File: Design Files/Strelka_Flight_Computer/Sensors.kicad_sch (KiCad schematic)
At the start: 0 parts

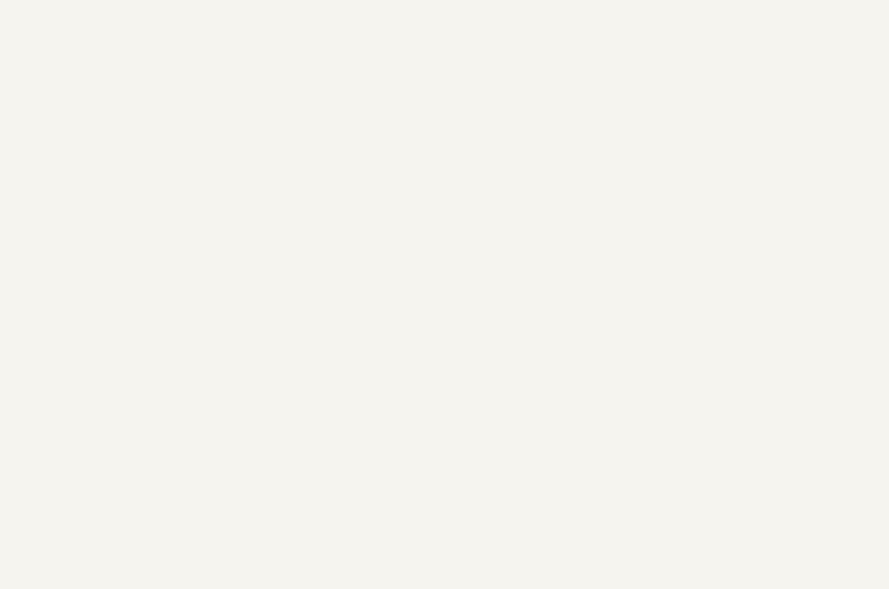
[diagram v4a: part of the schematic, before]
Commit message: Added new UBLOX GPS
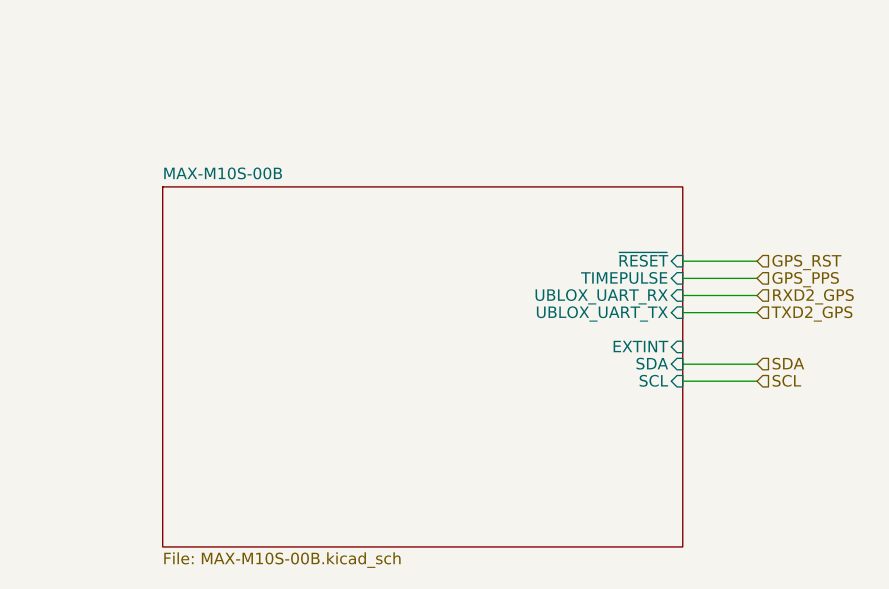
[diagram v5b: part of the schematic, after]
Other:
- added sheet MAX-M10S-00B (MAX-M10S-00B.kicad_sch)
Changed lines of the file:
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@@
+    (stroke (width 0) (type default) (color 0 0 0 0))
+  )
+  (wire (pts (xy 211.455 116.205) (xy 219.71 116.205))
     (stroke (width 0) (type default) (color 0 0 0 0))
   )
@@
     (stroke (width 0) (type default) (color 0 0 0 0))
   )
+  (wire (pts (xy 211.455 121.92) (xy 219.71 121.92))
+    (stroke (width 0) (type default) (color 0 0 0 0))
+  )
+  (wire (pts (xy 211.455 120.015) (xy 219.71 120.015))
+    (stroke (width 0) (type default) (color 0 0 0 0))
+  )
   (wire (pts (xy 95.25 41.275) (xy 103.505 41.275))
     (stroke (width 0) (type default) (color 0 0 0 0))
@@
     (stroke (width 0) (type default) (color 0 0 0 0))
   )
+  (wire (pts (xy 211.455 129.54) (xy 219.71 129.54))
+    (stroke (width 0) (type default) (color 0 0 0 0))
+  )
   (wire (pts (xy 95.25 134.62) (xy 103.505 134.62))
     (stroke (width 0) (type default) (color 0 0 0 0))
@@
     (stroke (width 0) (type default) (color 0 0 0 0))
   )
+  (wire (pts (xy 211.455 118.11) (xy 219.71 118.11))
+    (stroke (width 0) (type default) (color 0 0 0 0))
+  )
   (wire (pts (xy 211.455 43.815) (xy 219.71 43.815))
     (stroke (width 0) (type default) (color 0 0 0 0))
@@
     (stroke (width 0) (type default) (color 0 0 0 0))
   )
+  (wire (pts (xy 211.455 127.635) (xy 219.71 127.635))
+    (stroke (width 0) (type default) (color 0 0 0 0))
+  )
   (hierarchical_label "DATA_READY_MAG" (shape input) (at 103.505 136.525 0)
     (effects (font (size 1.27 1.27)) (justify left))
@@
     (effects (font (size 1.27 1.27)) (justify left))
   )
+  (hierarchical_label "RXD2_GPS" (shape input) (at 219.71 120.015 0)
+    (effects (font (size 1.27 1.27)) (justify left))
+  )
   (hierarchical_label "MOSI_BMX055" (shape input) (at 103.505 113.03 0)
     (effects (font (size 1.27 1.27)) (justify left))
@@
     (effects (font (size 1.27 1.27)) (justify left))
   )
+  (hierarchical_label "GPS_PPS" (shape input) (at 219.71 118.11 0)
+    (effects (font (size 1.27 1.27)) (justify left))
+  )
+  (hierarchical_label "SCL" (shape input) (at 219.71 129.54 0)
+    (effects (font (size 1.27 1.27)) (justify left))
+  )
+  (hierarchical_label "GPS_RST" (shape input) (at 219.71 116.205 0)
+    (effects (font (size 1.27 1.27)) (justify left))
+  )
+  (hierarchical_label "TXD2_GPS" (shape input) (at 219.71 121.92 0)
+    (effects (font (size 1.27 1.27)) (justify left))
+  )
   (hierarchical_label "GPS_PPS" (shape input) (at 219.71 41.91 0)
+    (effects (font (size 1.27 1.27)) (justify left))
+  )
+  (hierarchical_label "SDA" (shape input) (at 219.71 127.635 0)
     (effects (font (size 1.27 1.27)) (justify left))
   )
@@
       (effects (font (size 1.27 1.27)) (justify right))
     )
+  )
+  (sheet (at 153.67 107.95) (size 57.785 40.005) (fields_autoplaced)
+    (stroke (width 0.1524) (type solid) (color 0 0 0 0))
+    (fill (color 0 0 0 0.0000))
+    (property "Sheet name" "MAX-M10S-00B" (id 0) (at 153.67 107.2384 0)
+      (effects (font (size 1.27 1.27)) (justify left bottom))
+    )
+    (property "Sheet file" "MAX-M10S-00B.kicad_sch" (id 1) (at 153.67 148.5396 0)
+      (effects (font (size 1.27 1.27)) (justify left top))
+    )
+    (pin "SCL" input (at 211.455 129.54 0)
+      (effects (font (size 1.27 1.27)) (justify right))
+    )
+    (pin "SDA" input (at 211.455 127.635 0)
+      (effects (font (size 1.27 1.27)) (justify right))
+    )
+    (pin "UBLOX_UART_RX" input (at 211.455 120.015 0)
+      (effects (font (size 1.27 1.27)) (justify right))
+    )
+    (pin "~{RESET}" input (at 211.455 116.205 0)
+      (effects (font (size 1.27 1.27)) (justify right))
+    )
+    (pin "EXTINT" input (at 211.455 125.73 0)
+      (effects (font (size 1.27 1.27)) (justify right))
+    )
+    (pin "UBLOX_UART_TX" input (at 211.455 121.92 0)
+      (effects (font (size 1.27 1.27)) (justify right))
+    )
+    (pin "TIMEPULSE" input (at 211.455 118.11 0)
+      (effects (font (size 1.27 1.27)) (justify right))
+    )

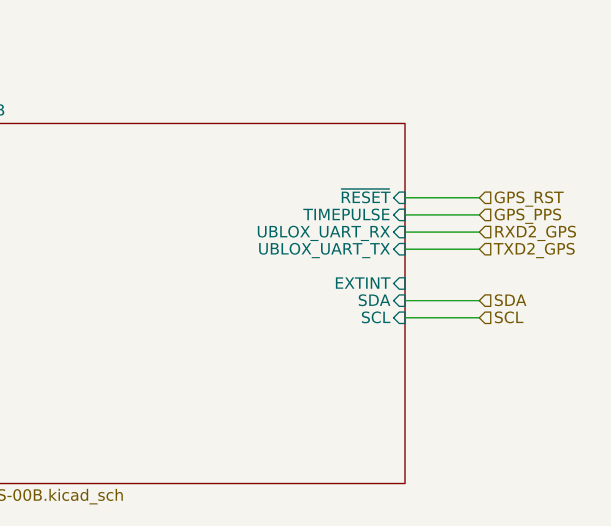
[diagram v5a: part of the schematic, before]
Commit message: Added motor driver to power board
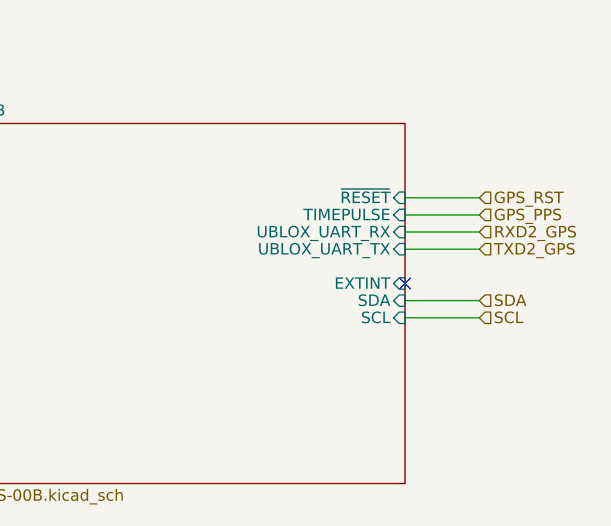
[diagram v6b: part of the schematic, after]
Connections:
- no-connect marks 0 -> 1
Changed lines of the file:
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@@
 (kicad_sch (version 20211123) (generator eeschema)
   (paper "A4")
+  (no_connect (at 211.455 125.73))
   (wire (pts (xy 95.25 113.03) (xy 103.505 113.03))
     (stroke (width 0) (type default) (color 0 0 0 0))

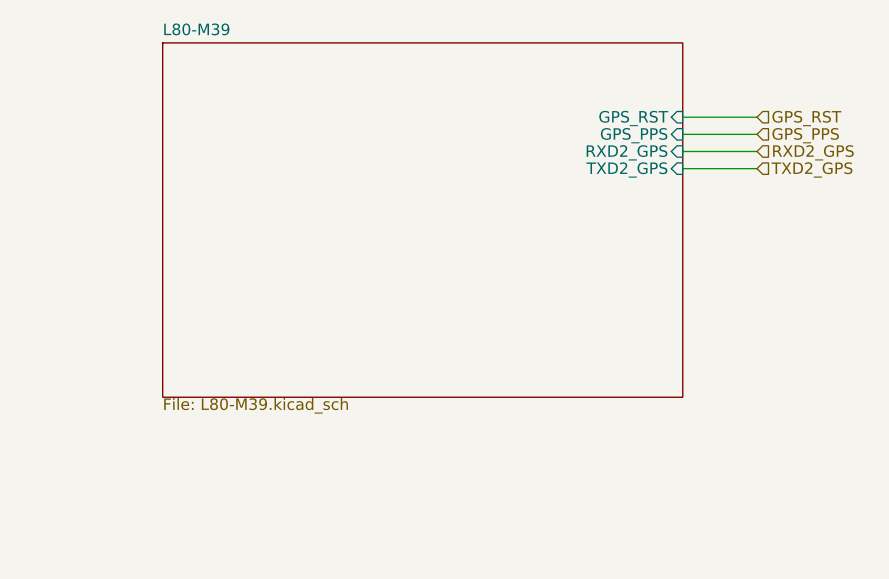
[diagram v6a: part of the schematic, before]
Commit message: Deleted extra boost circuit and L80 schematic
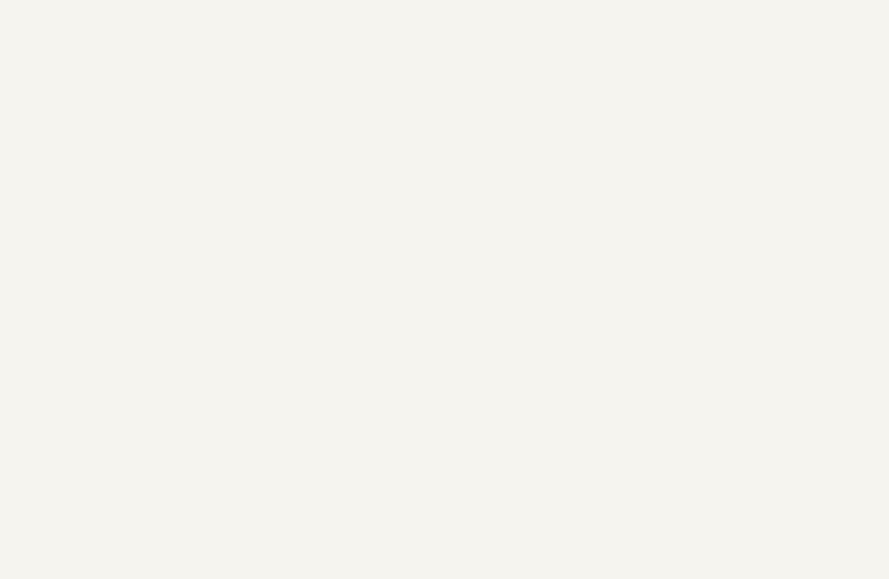
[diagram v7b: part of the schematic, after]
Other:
- removed sheet L80-M39
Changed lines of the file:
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@@
-    (stroke (width 0) (type default) (color 0 0 0 0))
-  )
-  (wire (pts (xy 211.455 40.005) (xy 219.71 40.005))
     (stroke (width 0) (type default) (color 0 0 0 0))
   )
@@
     (stroke (width 0) (type default) (color 0 0 0 0))
   )
-  (wire (pts (xy 211.455 41.91) (xy 219.71 41.91))
-    (stroke (width 0) (type default) (color 0 0 0 0))
-  )
   (wire (pts (xy 95.25 136.525) (xy 103.505 136.525))
-    (stroke (width 0) (type default) (color 0 0 0 0))
-  )
-  (wire (pts (xy 211.455 45.72) (xy 219.71 45.72))
     (stroke (width 0) (type default) (color 0 0 0 0))
   )
@@
   )
   (wire (pts (xy 211.455 118.11) (xy 219.71 118.11))
-    (stroke (width 0) (type default) (color 0 0 0 0))
-  )
-  (wire (pts (xy 211.455 43.815) (xy 219.71 43.815))
     (stroke (width 0) (type default) (color 0 0 0 0))
   )
@@
   )
   (hierarchical_label "INT_1_MAG" (shape input) (at 103.505 134.62 0)
-    (effects (font (size 1.27 1.27)) (justify left))
-  )
-  (hierarchical_label "GPS_RST" (shape input) (at 219.71 40.005 0)
-    (effects (font (size 1.27 1.27)) (justify left))
-  )
-  (hierarchical_label "TXD2_GPS" (shape input) (at 219.71 45.72 0)
     (effects (font (size 1.27 1.27)) (justify left))
   )
@@
   )
   (hierarchical_label "INT_1_GYRO" (shape input) (at 103.505 130.81 0)
-    (effects (font (size 1.27 1.27)) (justify left))
-  )
-  (hierarchical_label "RXD2_GPS" (shape input) (at 219.71 43.815 0)
     (effects (font (size 1.27 1.27)) (justify left))
   )
@@
     (effects (font (size 1.27 1.27)) (justify left))
   )
-  (hierarchical_label "GPS_PPS" (shape input) (at 219.71 41.91 0)
-    (effects (font (size 1.27 1.27)) (justify left))
-  )
   (hierarchical_label "SDA" (shape input) (at 219.71 127.635 0)
     (effects (font (size 1.27 1.27)) (justify left))
@@
     (effects (font (size 1.27 1.27)) (justify left))
   )
-  (sheet (at 153.67 31.75) (size 57.785 39.37) (fields_autoplaced)
-    (stroke (width 0.1524) (type solid) (color 0 0 0 0))
-    (fill (color 0 0 0 0.0000))
-    (property "Sheet name" "L80-M39" (id 0) (at 153.67 31.0384 0)
-      (effects (font (size 1.27 1.27)) (justify left bottom))
-    )
-    (property "Sheet file" "L80-M39.kicad_sch" (id 1) (at 153.67 71.1966 0)
-      (effects (font (size 0 0)) (justify left top))
-    )
-    (pin "GPS_RST" input (at 211.455 40.005 0)
-      (effects (font (size 1.27 1.27)) (justify right))
-    )
-    (pin "GPS_PPS" input (at 211.455 41.91 0)
-      (effects (font (size 1.27 1.27)) (justify right))
-    )
-    (pin "RXD2_GPS" input (at 211.455 43.815 0)
-      (effects (font (size 1.27 1.27)) (justify right))
-    )
-    (pin "TXD2_GPS" input (at 211.455 45.72 0)
-      (effects (font (size 1.27 1.27)) (justify right))
-    )
-  )
   (sheet (at 153.67 107.95) (size 57.785 40.005) (fields_autoplaced)

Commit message: PCB ordered
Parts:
- added TP10, TP6, TP7, TP8, TP9: TestPoint, TestPoint:TestPoint_Pad_1.0x1.0mm, symbol Connector:TestPoint
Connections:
- net MISO_BMX055: now also TP7.1
- net MOSI_BMX055: now also TP6.1
- net RXD2_GPS: now also TP10.1
- net SCK_BMX055: now also TP8.1
- net TXD2_GPS: now also TP9.1
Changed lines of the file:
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@@
 (kicad_sch (version 20211123) (generator eeschema)
   (paper "A4")
+  (junction (at 217.805 120.015) (diameter 0) (color 0 0 0 0)
+  )
+  (junction (at 97.155 113.03) (diameter 0) (color 0 0 0 0)
+  )
+  (junction (at 100.965 116.84) (diameter 0) (color 0 0 0 0)
+  )
+  (junction (at 212.725 121.92) (diameter 0) (color 0 0 0 0)
+  )
+  (junction (at 99.06 114.935) (diameter 0) (color 0 0 0 0)
+  )
   (no_connect (at 211.455 125.73))
-  (wire (pts (xy 95.25 113.03) (xy 103.505 113.03))
+  (wire (pts (xy 99.06 114.935) (xy 103.505 114.935))
+    (stroke (width 0) (type default) (color 0 0 0 0))
+  )
+  (wire (pts (xy 95.25 113.03) (xy 97.155 113.03))
     (stroke (width 0) (type default) (color 0 0 0 0))
   )
@@
     (stroke (width 0) (type default) (color 0 0 0 0))
   )
-  (wire (pts (xy 95.25 114.935) (xy 103.505 114.935))
+  (wire (pts (xy 95.25 114.935) (xy 99.06 114.935))
     (stroke (width 0) (type default) (color 0 0 0 0))
   )
@@
     (stroke (width 0) (type default) (color 0 0 0 0))
   )
+  (wire (pts (xy 100.965 116.84) (xy 103.505 116.84))
+    (stroke (width 0) (type default) (color 0 0 0 0))
+  )
+  (wire (pts (xy 99.06 103.505) (xy 99.06 114.935))
+    (stroke (width 0) (type default) (color 0 0 0 0))
+  )
+  (wire (pts (xy 217.805 120.015) (xy 219.71 120.015))
+    (stroke (width 0) (type default) (color 0 0 0 0))
+  )
   (wire (pts (xy 95.25 128.905) (xy 103.505 128.905))
     (stroke (width 0) (type default) (color 0 0 0 0))
   )
+  (wire (pts (xy 217.805 113.665) (xy 217.805 120.015))
+    (stroke (width 0) (type default) (color 0 0 0 0))
+  )
   (wire (pts (xy 95.25 45.085) (xy 103.505 45.085))
     (stroke (width 0) (type default) (color 0 0 0 0))
   )
-  (wire (pts (xy 211.455 121.92) (xy 219.71 121.92))
-    (stroke (width 0) (type default) (color 0 0 0 0))
-  )
-  (wire (pts (xy 211.455 120.015) (xy 219.71 120.015))
+  (wire (pts (xy 97.155 113.03) (xy 103.505 113.03))
+    (stroke (width 0) (type default) (color 0 0 0 0))
+  )
+  (wire (pts (xy 97.155 99.06) (xy 97.155 113.03))
+    (stroke (width 0) (type default) (color 0 0 0 0))
+  )
+  (wire (pts (xy 211.455 121.92) (xy 212.725 121.92))
+    (stroke (width 0) (type default) (color 0 0 0 0))
+  )
+  (wire (pts (xy 211.455 120.015) (xy 217.805 120.015))
     (stroke (width 0) (type default) (color 0 0 0 0))
   )
@@
     (stroke (width 0) (type default) (color 0 0 0 0))
   )
+  (wire (pts (xy 212.725 121.92) (xy 219.71 121.92))
+    (stroke (width 0) (type default) (color 0 0 0 0))
+  )
+  (wire (pts (xy 212.725 107.95) (xy 212.725 121.92))
+    (stroke (width 0) (type default) (color 0 0 0 0))
+  )
   (wire (pts (xy 95.25 136.525) (xy 103.505 136.525))
     (stroke (width 0) (type default) (color 0 0 0 0))
   )
-  (wire (pts (xy 95.25 116.84) (xy 103.505 116.84))
+  (wire (pts (xy 95.25 116.84) (xy 100.965 116.84))
     (stroke (width 0) (type default) (color 0 0 0 0))
   )
@@
     (stroke (width 0) (type default) (color 0 0 0 0))
   )
+  (wire (pts (xy 100.965 107.95) (xy 100.965 116.84))
+    (stroke (width 0) (type default) (color 0 0 0 0))
+  )
   (hierarchical_label "DATA_READY_MAG" (shape input) (at 103.505 136.525 0)
     (effects (font (size 1.27 1.27)) (justify left))
@@
     (effects (font (size 1.27 1.27)) (justify left))
   )
+  (symbol (lib_id "Connector:TestPoint") (at 212.725 107.95 0) (unit 1)
+    (in_bom yes) (on_board yes) (fields_autoplaced)
+    (property "Reference" "TP9" (id 0) (at 215.265 103.3779 0)
+      (effects (font (size 1.27 1.27)) (justify left))
+    )
+    (property "Value" "TestPoint" (id 1) (at 215.265 105.9179 0)
+      (effects (font (size 1.27 1.27)) (justify left))
+    )
+    (property "Footprint" "TestPoint:TestPoint_Pad_1.0x1.0mm" (id 2) (at 217.805 107.95 0)
+      (effects (font (size 1.27 1.27)) hide)
+    )
+    (property "Datasheet" "~" (id 3) (at 217.805 107.95 0)
+      (effects (font (size 1.27 1.27)) hide)
+    )
+    (pin "1")
+  )
+  (symbol (lib_id "Connector:TestPoint") (at 217.805 113.665 0) (unit 1)
+    (in_bom yes) (on_board yes) (fields_autoplaced)
+    (property "Reference" "TP10" (id 0) (at 220.345 109.0929 0)
+      (effects (font (size 1.27 1.27)) (justify left))
+    )
+    (property "Value" "TestPoint" (id 1) (at 220.345 111.6329 0)
+      (effects (font (size 1.27 1.27)) (justify left))
+    )
+    (property "Footprint" "TestPoint:TestPoint_Pad_1.0x1.0mm" (id 2) (at 222.885 113.665 0)
+      (effects (font (size 1.27 1.27)) hide)
+    )
+    (property "Datasheet" "~" (id 3) (at 222.885 113.665 0)
+      (effects (font (size 1.27 1.27)) hide)
+    )
+    (pin "1")
+  )
+  (symbol (lib_id "Connector:TestPoint") (at 100.965 107.95 0) (unit 1)
+    (in_bom yes) (on_board yes) (fields_autoplaced)
+    (property "Reference" "TP8" (id 0) (at 103.505 103.3779 0)
+      (effects (font (size 1.27 1.27)) (justify left))
+    )
+    (property "Value" "TestPoint" (id 1) (at 103.505 105.9179 0)
+      (effects (font (size 1.27 1.27)) (justify left))
+    )
+    (property "Footprint" "TestPoint:TestPoint_Pad_1.0x1.0mm" (id 2) (at 106.045 107.95 0)
+      (effects (font (size 1.27 1.27)) hide)
+    )
+    (property "Datasheet" "~" (id 3) (at 106.045 107.95 0)
+      (effects (font (size 1.27 1.27)) hide)
+    )
+    (pin "1")
+  )
+  (symbol (lib_id "Connector:TestPoint") (at 99.06 103.505 0) (unit 1)
+    (in_bom yes) (on_board yes) (fields_autoplaced)
+    (property "Reference" "TP7" (id 0) (at 101.6 98.9329 0)
+      (effects (font (size 1.27 1.27)) (justify left))
+    )
+    (property "Value" "TestPoint" (id 1) (at 101.6 101.4729 0)
+      (effects (font (size 1.27 1.27)) (justify left))
+    )
+    (property "Footprint" "TestPoint:TestPoint_Pad_1.0x1.0mm" (id 2) (at 104.14 103.505 0)
+      (effects (font (size 1.27 1.27)) hide)
+    )
+    (property "Datasheet" "~" (id 3) (at 104.14 103.505 0)
+      (effects (font (size 1.27 1.27)) hide)
+    )
+    (pin "1")
+  )
+  (symbol (lib_id "Connector:TestPoint") (at 97.155 99.06 0) (unit 1)
+    (in_bom yes) (on_board yes) (fields_autoplaced)
+    (property "Reference" "TP6" (id 0) (at 99.695 94.4879 0)
+      (effects (font (size 1.27 1.27)) (justify left))
+    )
+    (property "Value" "TestPoint" (id 1) (at 99.695 97.0279 0)
+      (effects (font (size 1.27 1.27)) (justify left))
+    )
+    (property "Footprint" "TestPoint:TestPoint_Pad_1.0x1.0mm" (id 2) (at 102.235 99.06 0)
+      (effects (font (size 1.27 1.27)) hide)
+    )
+    (property "Datasheet" "~" (id 3) (at 102.235 99.06 0)
+      (effects (font (size 1.27 1.27)) hide)
+    )
+    (pin "1")
+  )
   (sheet (at 153.67 107.95) (size 57.785 40.005) (fields_autoplaced)
